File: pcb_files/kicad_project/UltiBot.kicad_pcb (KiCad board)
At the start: 2 copper layers, 87 x 48 mm, 67 parts, among them IC1 AS5145B-HSST, IC2 AS5145B-HSST, J1 Conn_01x03_Pin, J10 Conn_01x04_Pin, J11 Conn_01x05_Pin, J12 Conn_01x05_Pin, J13 Conn_01x05_Pin, J14 Conn_01x05_Pin, J15 Conn_01x05_Pin, J16 Conn_01x05_Pin, J17 Conn_01x03_Pin, J18 Conn_01x03_Pin, J2 Conn_01x03_Pin, J3 Conn_01x03_Pin, J4 Conn_01x03_Pin, J5 Conn_01x03_Pin, J6 Conn_01x03_Pin, J7 Conn_01x03_Pin, J8 Conn_01x03_Pin, J9 Conn_01x04_Pin, U2 BluePill, Y1 Crystal

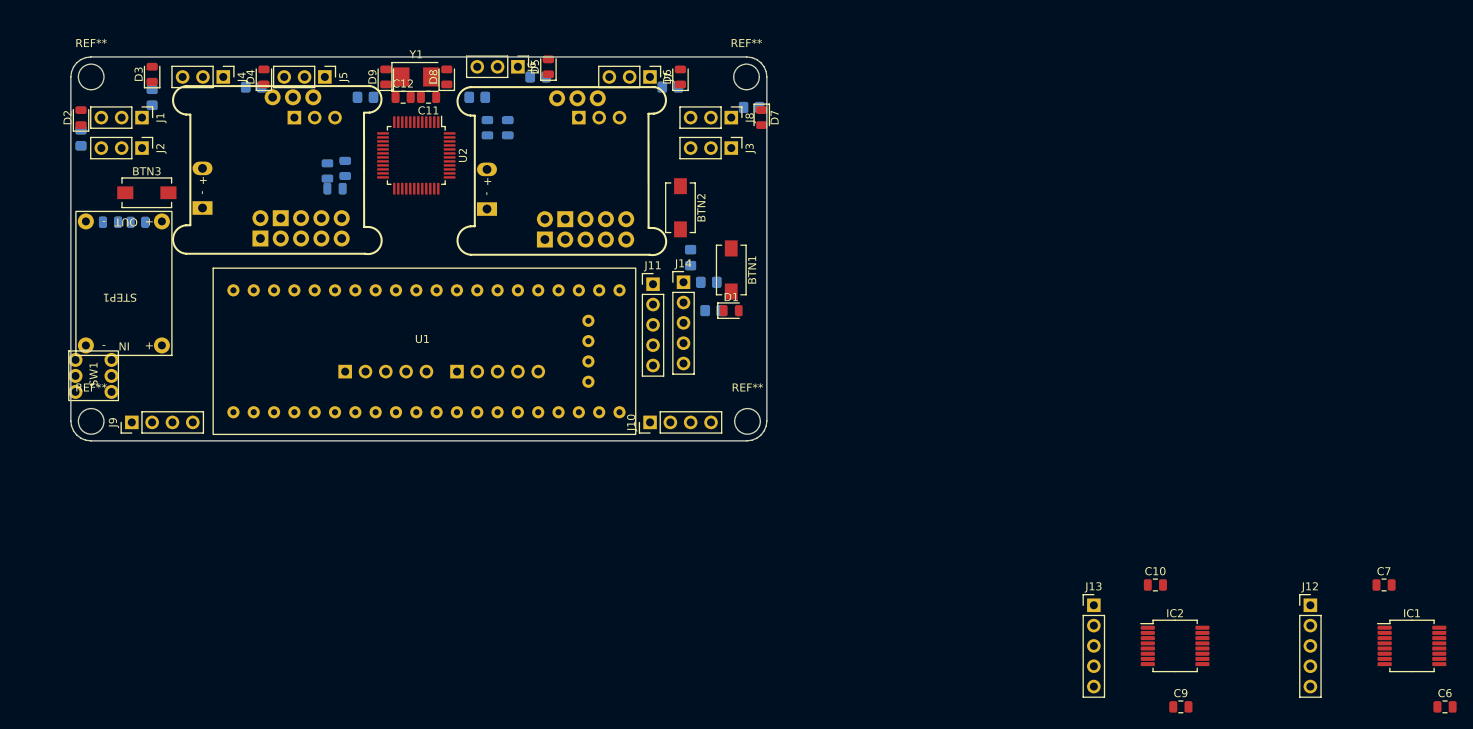
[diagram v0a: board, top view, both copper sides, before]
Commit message: Actualiza esquemático y finaliza ruteado de PCB
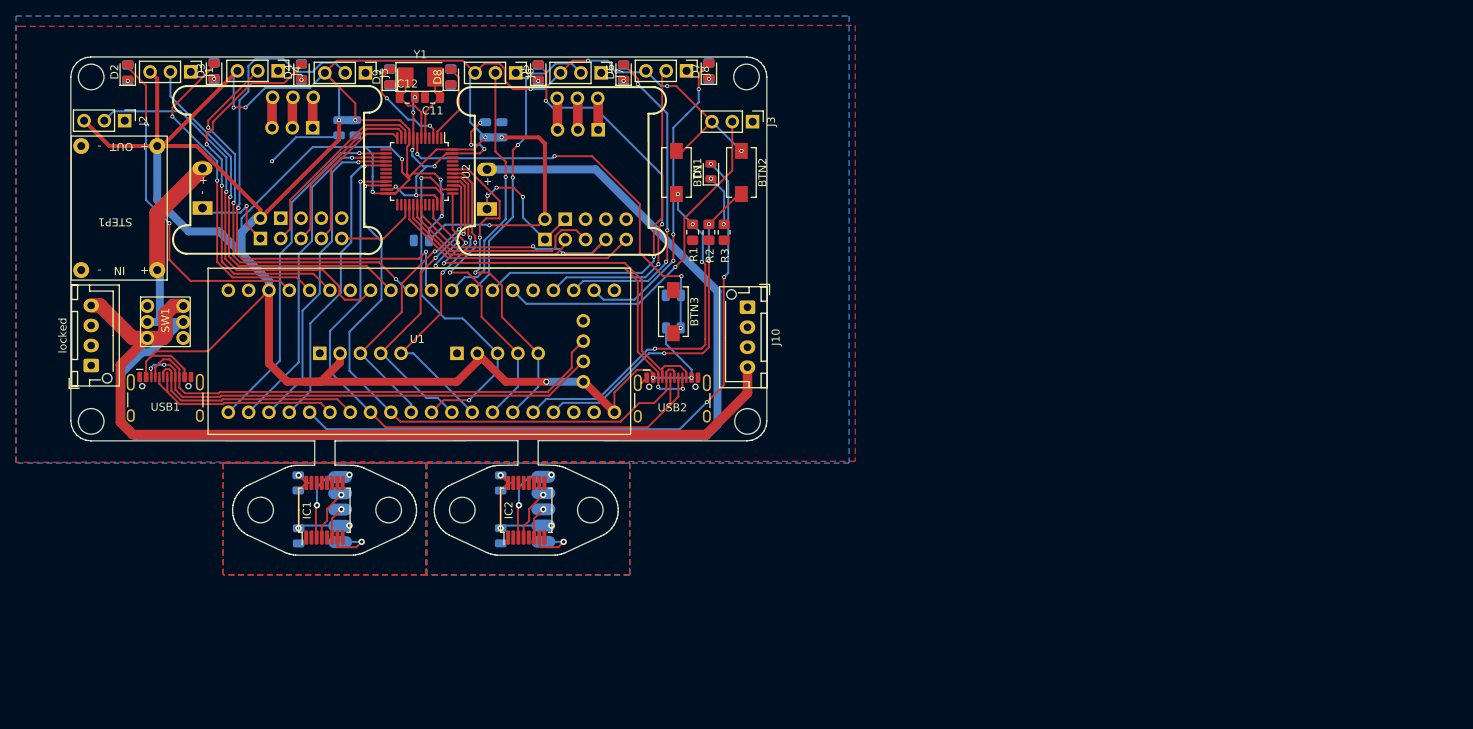
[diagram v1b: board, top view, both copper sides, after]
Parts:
- removed the J11 at (174.4, 76.7)
- removed the J14 at (178.2, 76.5)
- added REF**: MountingHole_3.2mm_M3, MountingHole:MountingHole_3.2mm_M3, F.Cu at (166.5, 104.9)
- added REF**: MountingHole_3.2mm_M3, MountingHole:MountingHole_3.2mm_M3, F.Cu at (125.3, 104.9)
- added REF**: MountingHole_3.2mm_M3, MountingHole:MountingHole_3.2mm_M3, F.Cu at (150.5, 104.9)
- added REF**: MountingHole_3.2mm_M3, MountingHole:MountingHole_3.2mm_M3, F.Cu at (141.3, 104.9)
- added USB1: ~, custom_footprints:USB-C ST-Link USART, F.Cu at (113.4, 92.1)
- added USB2: ~, custom_footprints:USB-C ST-Link USART, F.Cu at (176.8, 92.1)
- C10, C6, C7, C9: moved to B.Cu
- J10: footprint Connector_PinHeader_2.54mm:PinHeader_1x04_P2.54mm_Vertical -> Connector_JST:JST_XH_B4B-XH-AM_1x04_P2.50mm_Vertical
- J11: renamed from J12; moved to B.Cu
- J12: renamed from J13; moved to B.Cu
- R1, R2, R3: moved to F.Cu
- locked: renamed from J9; footprint Connector_PinHeader_2.54mm:PinHeader_1x04_P2.54mm_Vertical -> Connector_JST:JST_XH_B4B-XH-AM_1x04_P2.50mm_Vertical
- moved C6 144.9 mm to (130.1, 108.2), turned to -90 degrees
- moved IC1 137.0 mm to (133.3, 105.0), turned to 90 degrees
- moved C7 136.3 mm to (130.0, 101.5), turned to -90 degrees
- moved J11 121.5 mm to (135.3, 110.0)
- moved C9 87.7 mm to (155.3, 108.1), turned to -90 degrees
- moved IC2 82.9 mm to (158.5, 105.0), turned to 90 degrees
- moved C10 82.8 mm to (155.3, 101.5), turned to -90 degrees
- moved C3 70.9 mm to (176.9, 78.1)
- moved J12 69.3 mm to (160.7, 108.9)
- moved R10 68.2 mm to (176.9, 82.2), turned to 180 degrees
- moved BTN3 67.5 mm to (176.9, 80.1), turned to -90 degrees
- moved J15 38.0 mm to (167.5, 57.4), turned to 90 degrees
- moved J16 33.3 mm to (131.8, 57.1), turned to 90 degrees
- moved C5 22.4 mm to (155.4, 57.4)
- moved C2 19.1 mm to (137.2, 57.1)
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- renumbered J15 to J13, J16 to J14, J17 to J15, J18 to J16
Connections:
- C1 pad 1: +3.3V -> +3V3
- C2 pad 1: +3.3V -> +3V3
- C4 pad 1: +3.3V -> +3V3
- C5 pad 1: +3.3V -> +3V3
- C8 pad 1: +3.3V -> +3V3
- J13 pad 2: +3.3V -> +3V3
- J14 pad 2: +3.3V -> +3V3
- J15 pad 3: /BluePill&FOC/M1_B_CONN -> /BluePill&FOC/M1_C_CONN
- J16 pad 3: /BluePill&FOC/M2_B_CONN -> /BluePill&FOC/M2_C_CONN
- R10 pad 2: +3.3V -> +3V3
- STEP1 pad 1: Net-(STEP1-IN+) -> /BlackPill&Main/+12V_SW
- SW1 pad 2: Net-(STEP1-IN+) -> /BlackPill&Main/+12V_SW
- SW1 pad 5: Net-(STEP1-IN+) -> /BlackPill&Main/+12V_SW
- U2 pad 24: +3.3V -> +3V3
- U2 pad 36: +3.3V -> +3V3
- U2 pad 48: +3.3V -> +3V3
- U2 pad 9: +3.3V -> +3V3
- U3 pad 15: +3.3V -> +3V3
- U3 pad 3: /BluePill&FOC/M1_B_CONN -> /BluePill&FOC/M1_C_CONN
- U3 pad 4: +12V -> /BlackPill&Main/+12V_SW
- U4 pad 15: +3.3V -> +3V3
- U4 pad 3: /BluePill&FOC/M2_B_CONN -> /BluePill&FOC/M2_C_CONN
- U4 pad 4: +12V -> /BlackPill&Main/+12V_SW
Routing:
- net +3V3: track 0.00 -> 448.9 mm, vias 0 -> 18
- net /BlackPill&Main/+12V_SW: track 0.00 -> 171.7 mm
- net +12V: track 0.00 -> 112.8 mm
- net /BlackPill&Main/LED_0: track 0.00 -> 83.7 mm, vias 0 -> 3
- net /BlackPill&Main/USART6_TX: track 0.00 -> 82.8 mm, vias 0 -> 1
- net /BlackPill&Main/USART6_RX: track 0.00 -> 76.5 mm, vias 0 -> 1
- net GND: track 0.00 -> 75.0 mm, vias 0 -> 14
- net /BlackPill&Main/SENSOR_3: track 0.00 -> 67.5 mm, vias 0 -> 2
- net /BlackPill&Main/SWCLK: track 0.00 -> 62.1 mm
- net /BlackPill&Main/SWDIO: track 0.00 -> 60.3 mm, vias 0 -> 2
- net /BluePill&FOC/SWDIO: track 0.00 -> 55.1 mm, vias 0 -> 4
- net /BluePill&FOC/SWCLK: track 0.00 -> 54.9 mm, vias 0 -> 2
- net /BluePill&FOC/RESET: track 0.00 -> 52.8 mm, vias 0 -> 4
- net /BlackPill&Main/SENSOR_LINEA_1: track 0.00 -> 52.2 mm, vias 0 -> 1
- net /BlackPill&Main/SENSOR_2: track 0.00 -> 51.2 mm, vias 0 -> 3
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- added copper zone on B.Cu, net /BluePill&FOC/ENC_1_GND
- added copper zone on F.Cu, net /BluePill&FOC/ENC_1_GND
- added copper zone on B.Cu, net /BluePill&FOC/ENC_2_GND
- added copper zone on F.Cu, net /BluePill&FOC/ENC_2_GND
- added copper zone on B.Cu, net GND
- added copper zone on F.Cu, net GND
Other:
- board size 87 x 48 mm -> 87 x 62.3 mm
- board text added: "A"
- board text added: "B"
- board text added: "G"
- board text added: "I"
- board text added: "V"

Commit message: Termina el diseño del esquemático y PCB
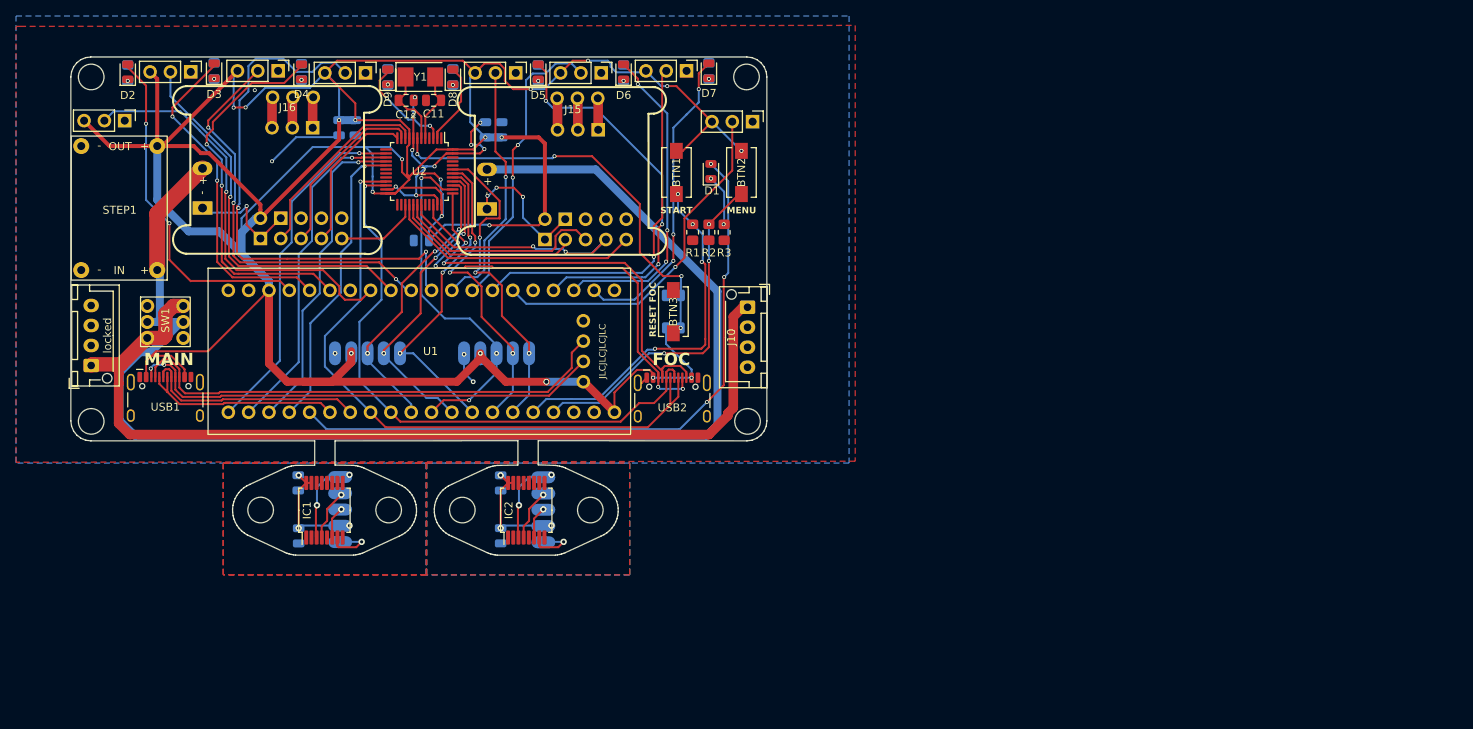
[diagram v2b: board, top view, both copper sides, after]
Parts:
- added G***: LOGO, LOGO, B.Cu at (110.6, 67.1)
- added G***: LOGO, LOGO, B.Cu at (145.3, 64.4)
- added G***: LOGO, LOGO, B.Cu at (181.1, 67.2)
- BTN1, BTN2, BTN3: footprint Button_Switch_SMD:SW_SPST_EVQPE1 -> custom_footprints:BTN_SMD_3x6x2.5mm
- J1, J15, J16, J2, J3, J4, J5, J6, J7, J8: footprint Connector_PinHeader_2.54mm:PinHeader_1x03_P2.54mm_Vertical -> custom_footprints:PinHeader_1x03_P2.54mm_Vertical_NoPins
- J10, locked: footprint Connector_JST:JST_XH_B4B-XH-AM_1x04_P2.50mm_Vertical -> custom_footprints:JST - XH - Thru (V) - 4Pin - 2.54mm
- J11, J12, J13, J14: footprint Connector_PinHeader_2.54mm:PinHeader_1x05_P2.54mm_Vertical -> custom_footprints:1x05 Pad
- Y1: footprint Crystal:Crystal_SMD_5032-2Pin_5.0x3.2mm -> custom_footprints:Crystal_SMD_5032-2Pin_5.0x3.2mm
- moved J12 1.07 mm to (160.7, 110.0)
- moved J14 0.89 mm to (133.6, 85.3)
- moved C12 0.41 mm to (143.5, 53.7)
- moved C11 0.40 mm to (146.9, 53.7)
- moved D9 0.25 mm to (141.2, 50.8)
- moved R12 0.25 mm to (141.2, 50.8)
- moved D8 0.25 mm to (149.4, 50.8)
- moved R11 0.25 mm to (149.4, 50.8)
- moved J13 0.13 mm to (149.7, 85.3)
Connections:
- J10 pad 1: GND -> +12V
- J10 pad 4: +12V -> GND
- locked pad 1: GND -> +12V
- locked pad 4: +12V -> GND
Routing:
- net +12V: track 112.8 -> 121.0 mm
- net GND: track 75.0 -> 83.1 mm, vias 14 -> 18
- net +3V3: track 448.9 -> 451.0 mm, vias 18 -> 20
- net /BlackPill&Main/USART6_RX: track 76.5 -> 75.5 mm
- net /BlackPill&Main/ENC_1_A: track 41.7 -> 40.8 mm, vias 2 -> 3
- net /BlackPill&Main/ENC_2_I: track 37.3 -> 36.6 mm, vias 2 -> 3
- net /BlackPill&Main/ENC_1_B: track 39.2 -> 38.7 mm, vias 2 -> 3
- net /BlackPill&Main/USART6_TX: track 82.8 -> 83.3 mm
- net /BlackPill&Main/ENC_1_I: track 44.4 -> 44.8 mm, vias 2 -> 3
- net /BlackPill&Main/ENC_2_B: track 39.2 -> 38.9 mm, vias 2 -> 3
- net /BlackPill&Main/ENC_2_A: track 39.1 -> 39.3 mm, vias 2 -> 3
- net Net-(D8-K): track 0.00 -> 0.06 mm, vias 0 -> 1
- net Net-(D9-K): vias 0 -> 1
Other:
- board text added: "A VER SE NON ARDE..."
- board text added: "Diseñado por @robotaleh"
- board text added: "E SE ARDE, QUE ARDA!"
- board text added: "FOC"
- board text added: "GitHub.com/OPRobots/UltiBot"
- board text added: "JLCJLCJLCJLC"
- board text added: "MAIN"
- board text added: "MENU"
- board text added: "RESET FOC"
- board text added: "START"

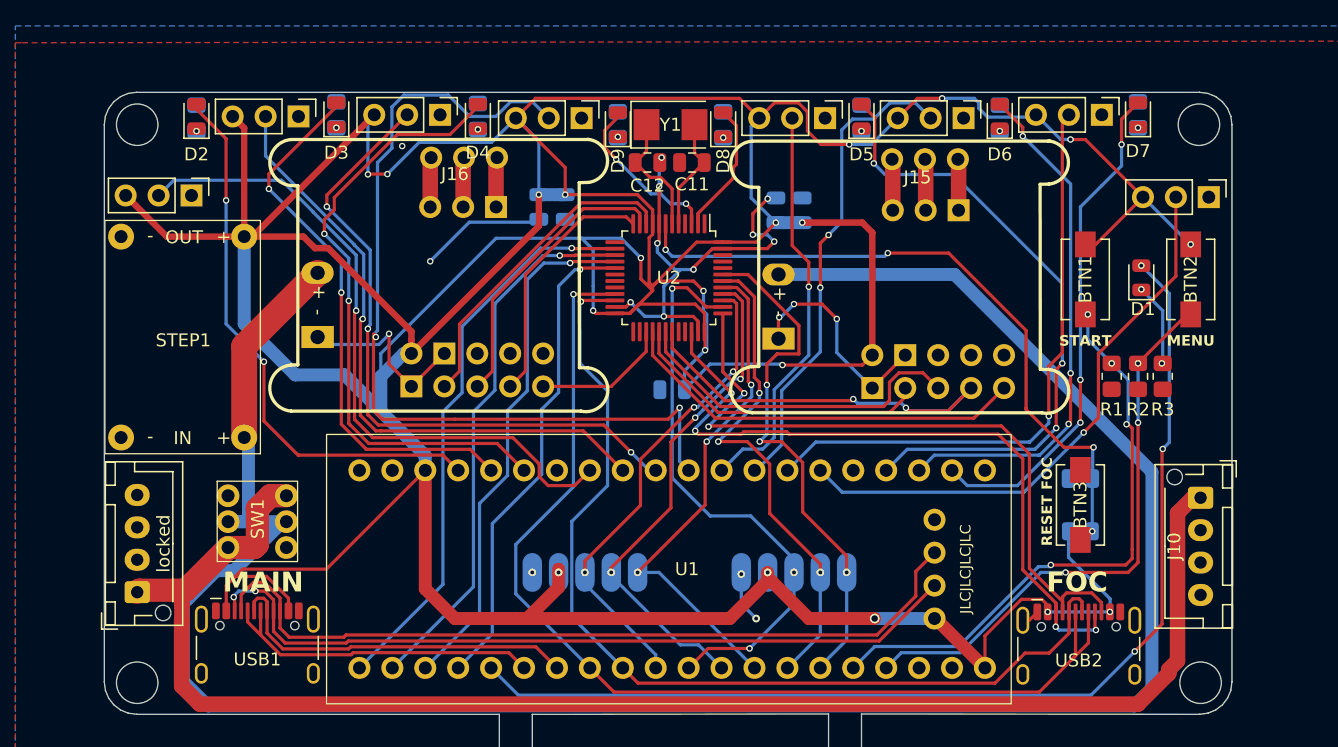
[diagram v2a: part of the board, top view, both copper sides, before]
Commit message: Corrige USART6 RX<>TX en la BluePill
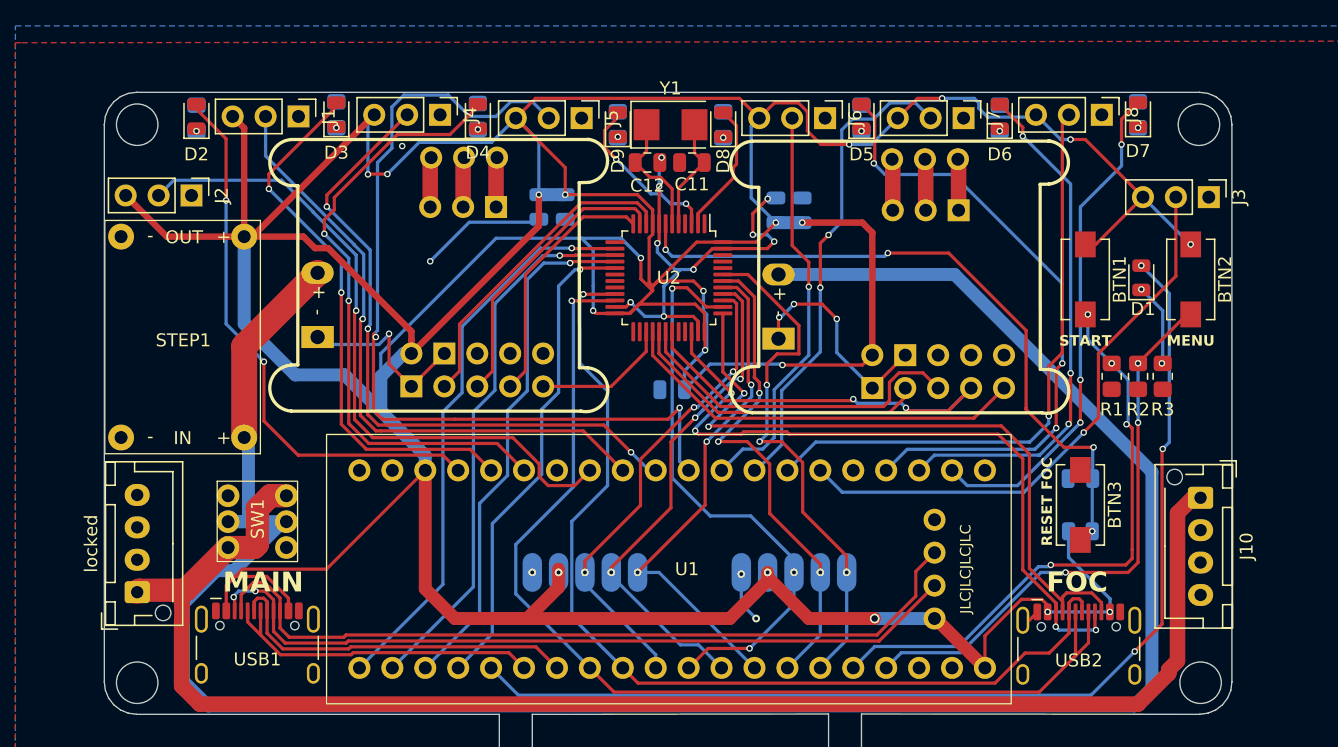
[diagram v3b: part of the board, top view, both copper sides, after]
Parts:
- BTN1, BTN2, BTN3: footprint custom_footprints:BTN_SMD_3x6x2.5mm -> Button_Switch_SMD:SW_SPST_EVQPE1
- J1, J15, J16, J2, J3, J4, J5, J6, J7, J8: footprint custom_footprints:PinHeader_1x03_P2.54mm_Vertical_NoPins -> Connector_PinHeader_2.54mm:PinHeader_1x03_P2.54mm_Vertical
- J10, locked: footprint custom_footprints:JST - XH - Thru (V) - 4Pin - 2.54mm -> Connector_JST:JST_XH_B4B-XH-AM_1x04_P2.50mm_Vertical
- Y1: footprint custom_footprints:Crystal_SMD_5032-2Pin_5.0x3.2mm -> Crystal:Crystal_SMD_5032-2Pin_5.0x3.2mm
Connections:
- U2 pad 21: /BlackPill&Main/USART6_TX -> /BlackPill&Main/USART6_RX
- U2 pad 22: /BlackPill&Main/USART6_RX -> /BlackPill&Main/USART6_TX
